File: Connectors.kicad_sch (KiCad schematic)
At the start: 3 parts, among them J1 A, J2 B, J3 C

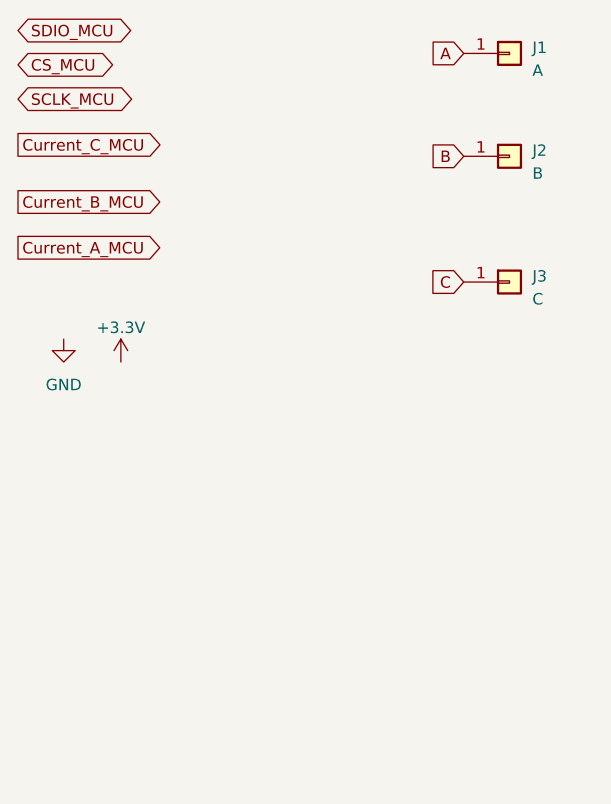
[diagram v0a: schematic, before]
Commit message: Изменил контур под новую крышку
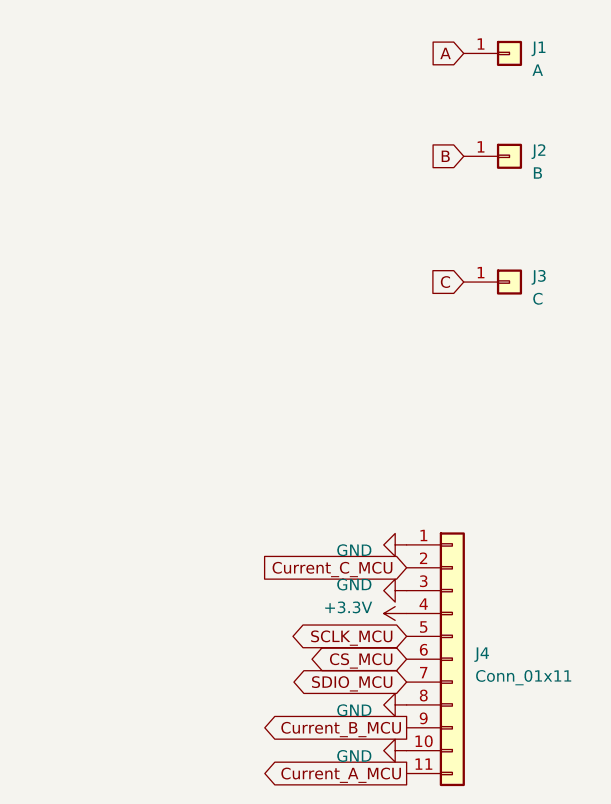
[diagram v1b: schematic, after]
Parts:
- added J4: Conn_01x11, Connector_PinHeader_2.54mm:PinHeader_1x11_P2.54mm_Vertical, symbol Connector_Generic:Conn_01x11
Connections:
- net +3.3V: now also J4.4 (Pin_4)
- net CS_MCU: now also J4.6 (Pin_6)
- net Current_A_MCU: now also J4.11 (Pin_11)
- net Current_B_MCU: now also J4.9 (Pin_9)
- net Current_C_MCU: now also J4.2 (Pin_2)
- net GND: now also J4.1 (Pin_1), J4.10 (Pin_10), J4.3 (Pin_3), J4.8 (Pin_8)
- net SCLK_MCU: now also J4.5 (Pin_5)
- net SDIO_MCU: now also J4.7 (Pin_7)

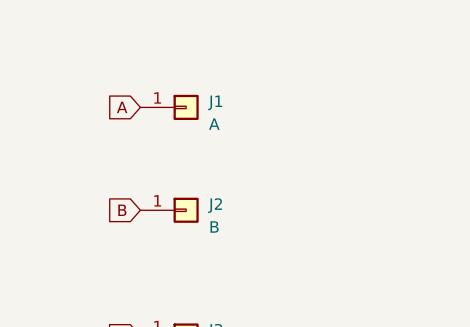
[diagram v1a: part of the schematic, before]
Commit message: Добавил разъёмы под обмотку
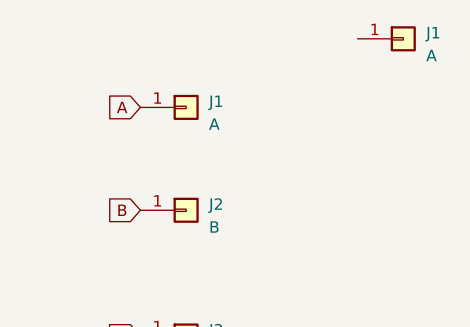
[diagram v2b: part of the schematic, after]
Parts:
- added J1: A, Connector_My:Power_Wire, symbol Connector_Generic:Conn_01x01
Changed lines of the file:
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@@
+    )
+  )
+  (symbol (lib_id "Connector_Generic:Conn_01x01") (at 135.89 73.66 0) (unit 1)
+    (in_bom yes) (on_board yes) (dnp no) (fields_autoplaced)
+    (property "Reference" "J1" (at 138.43 73.025 0)
+      (effects (font (size 1.27 1.27)) (justify left))
+    )
+    (property "Value" "A" (at 138.43 75.565 0)
+      (effects (font (size 1.27 1.27)) (justify left))
+    )
+    (property "Footprint" "Connector_My:Power_Wire" (at 135.89 73.66 0)
+      (effects (font (size 1.27 1.27)) hide)
+    )
+    (property "Datasheet" "~" (at 135.89 73.66 0)
+      (effects (font (size 1.27 1.27)) hide)
+    )
+    (pin "1")
+    (instances
+      (project "Плата датчиков"
+        (path "/69677e3f-3942-4c93-9a5c-92669e2df5eb"
+          (reference "J1") (unit 1)
+        )
+        (path "/69677e3f-3942-4c93-9a5c-92669e2df5eb/000644ca-6534-4b7d-8782-682dfa02d17c"
+          (reference "J5") (unit 1)
+        )
+      )
     )
   )

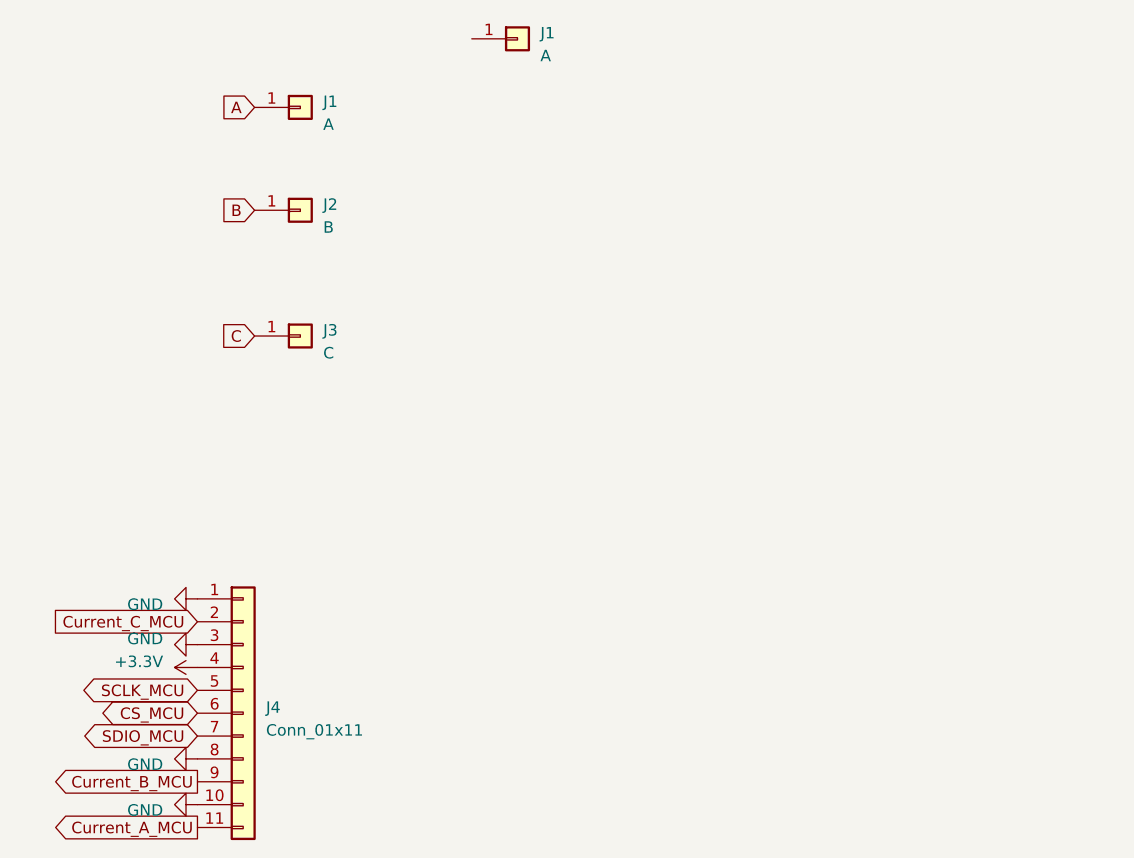
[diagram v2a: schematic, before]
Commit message: Переместил силовые разъёмы
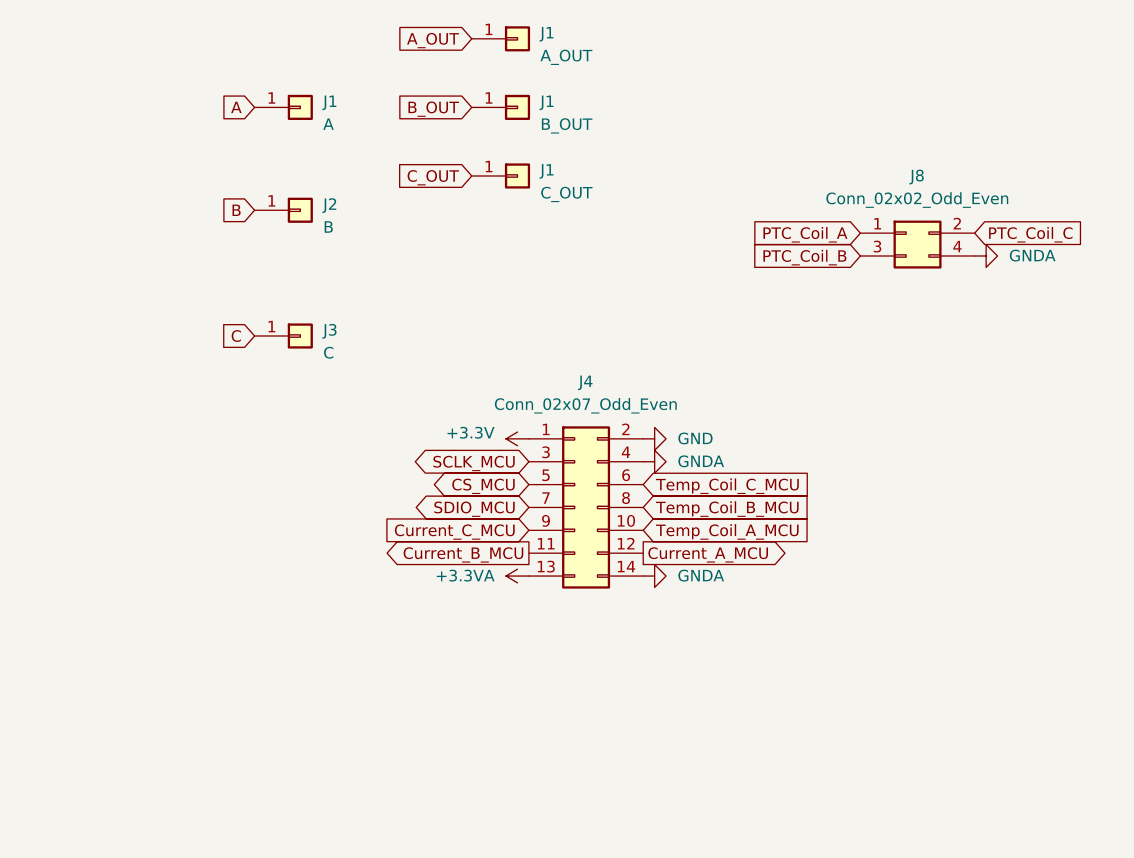
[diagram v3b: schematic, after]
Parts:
- removed J4: Conn_01x11, Connector_PinHeader_2.54mm:PinHeader_1x11_P2.54mm_Vertical, symbol Connector_Generic:Conn_01x11
- added J1: B_OUT, Connector_My:Power_Wire, symbol Connector_Generic:Conn_01x01
- added J1: C_OUT, Connector_My:Power_Wire, symbol Connector_Generic:Conn_01x01
- added J4: Conn_02x07_Odd_Even, Connector_PinSocket_2.54mm:PinSocket_2x07_P2.54mm_Vertical, symbol Connector_Generic:Conn_02x07_Odd_Even
- added J8: Conn_02x02_Odd_Even, Connector_PinHeader_2.54mm:PinHeader_2x02_P2.54mm_Vertical, symbol Connector_Generic:Conn_02x02_Odd_Even
- J1: value A -> A_OUT
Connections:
- net +3.3V: now also J4.1 (Pin_1)
- net CS_MCU: now also J4.5 (Pin_5)
- net Current_A_MCU: now also J4.12 (Pin_12)
- net Current_B_MCU: now also J4.11 (Pin_11)
- net Current_C_MCU: now also J4.9 (Pin_9)
- net GND: now also J4.2 (Pin_2)
- net SCLK_MCU: now also J4.3 (Pin_3)
- net SDIO_MCU: now also J4.7 (Pin_7)
- net A_OUT: now reaches J1.1 (Pin_1)
- new net +3.3VA: J4.13 (Pin_13)
- new net B_OUT: J1.1 (Pin_1)
- new net C_OUT: J1.1 (Pin_1)
- new net GNDA: J4.14 (Pin_14), J4.4 (Pin_4), J8.4 (Pin_4)
- new net PTC_Coil_A: J8.1 (Pin_1)
- new net PTC_Coil_B: J8.3 (Pin_3)
- new net PTC_Coil_C: J8.2 (Pin_2)
- new net Temp_Coil_A_MCU: J4.10 (Pin_10)
- new net Temp_Coil_B_MCU: J4.8 (Pin_8)
- new net Temp_Coil_C_MCU: J4.6 (Pin_6)

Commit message: С ножевыми разъёмами по кругу
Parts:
- removed J1: A_OUT, Connector_My:Power_Wire, symbol Connector_Generic:Conn_01x01
- removed J1: B_OUT, Connector_My:Power_Wire, symbol Connector_Generic:Conn_01x01
- removed J1: C_OUT, Connector_My:Power_Wire, symbol Connector_Generic:Conn_01x01
- added J10, J11, J12, J13, J14, J5, J6, J7, J9: 4900, Connector_My:4900, symbol 4900:4900
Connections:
- net A_OUT: now also J5.1, J5.2, J6.1, J6.2, J9.1, J9.2
- net B_OUT: now also J10.1, J10.2, J11.1, J11.2, J7.1, J7.2
- net C_OUT: now also J12.1, J12.2, J13.1, J13.2, J14.1, J14.2

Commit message: Ещё доработать
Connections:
- net B_OUT: now also J12.1, J12.2, J13.1, J13.2, J14.1, J14.2; no longer J10.1, J10.2, J11.1, J11.2, J7.1, J7.2
- net CS_MCU: now also J4.3 (Pin_3); no longer J4.5 (Pin_5)
- net C_OUT: now also J10.1, J10.2, J11.1, J11.2, J7.1, J7.2; no longer J12.1, J12.2, J13.1, J13.2, J14.1, J14.2
- net Current_C_MCU: now also J4.10 (Pin_10); no longer J4.9 (Pin_9)
- net GNDA: no longer J4.4 (Pin_4)
- net SCLK_MCU: now also J4.5 (Pin_5); no longer J4.3 (Pin_3)
- net Temp_Coil_A_MCU: now also J4.8 (Pin_8); no longer J4.10 (Pin_10)
- net Temp_Coil_B_MCU: now also J4.6 (Pin_6); no longer J4.8 (Pin_8)
- net Temp_Coil_C_MCU: now also J4.4 (Pin_4); no longer J4.6 (Pin_6)
- new net OUT_MCU: J4.9 (Pin_9)

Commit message: Собираю документацию
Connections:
- net GNDA: now also J8.2 (Pin_2); no longer J8.4 (Pin_4)
- net PTC_Coil_B: now also J8.4 (Pin_4); no longer J8.3 (Pin_3)
- net PTC_Coil_C: now also J8.3 (Pin_3); no longer J8.2 (Pin_2)
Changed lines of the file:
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@@
     )
   )
-  (global_label "PTC_Coil_C" (shape input) (at 186.69 95.25 0) (fields_autoplaced)
-    (effects (font (size 1.27 1.27)) (justify left))
-    (property "Intersheetrefs" "${INTERSHEET_REFS}" (at 200.077 95.25 0)
-      (effects (font (size 1.27 1.27)) (justify left) hide)
+  (global_label "PTC_Coil_C" (shape input) (at 173.99 97.79 180) (fields_autoplaced)
+    (effects (font (size 1.27 1.27)) (justify right))
+    (property "Intersheetrefs" "${INTERSHEET_REFS}" (at 160.603 97.79 0)
+      (effects (font (size 1.27 1.27)) (justify right) hide)
     )
   )
@@
     )
   )
-  (global_label "PTC_Coil_B" (shape input) (at 173.99 97.79 180) (fields_autoplaced)
-    (effects (font (size 1.27 1.27)) (justify right))
-    (property "Intersheetrefs" "${INTERSHEET_REFS}" (at 160.603 97.79 0)
-      (effects (font (size 1.27 1.27)) (justify right) hide)
+  (global_label "PTC_Coil_B" (shape input) (at 186.69 97.79 0) (fields_autoplaced)
+    (effects (font (size 1.27 1.27)) (justify left))
+    (property "Intersheetrefs" "${INTERSHEET_REFS}" (at 200.077 97.79 0)
+      (effects (font (size 1.27 1.27)) (justify left) hide)
     )
   )
@@
     )
   )
-  (symbol (lib_id "power:GNDA") (at 186.69 97.79 90) (unit 1)
-    (in_bom yes) (on_board yes) (dnp no) (fields_autoplaced)
-    (property "Reference" "#PWR038" (at 193.04 97.79 0)
-      (effects (font (size 1.27 1.27)) hide)
-    )
-    (property "Value" "GNDA" (at 190.5 97.79 90)
+  (symbol (lib_id "power:GNDA") (at 186.69 95.25 90) (unit 1)
+    (in_bom yes) (on_board yes) (dnp no) (fields_autoplaced)
+    (property "Reference" "#PWR038" (at 193.04 95.25 0)
+      (effects (font (size 1.27 1.27)) hide)
+    )
+    (property "Value" "GNDA" (at 190.5 95.25 90)
       (effects (font (size 1.27 1.27)) (justify right))
     )
-    (property "Footprint" "" (at 186.69 97.79 0)
-      (effects (font (size 1.27 1.27)) hide)
-    )
-    (property "Datasheet" "" (at 186.69 97.79 0)
-      (effects (font (size 1.27 1.27)) hide)
-    )
+    (property "Footprint" "" (at 186.69 95.25 0)
+      (effects (font (size 1.27 1.27)) hide)
+    )
+    (property "Datasheet" "" (at 186.69 95.25 0)
+      (effects (font (size 1.27 1.27)) hide)
+    )

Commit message: ...
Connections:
- net A_OUT: now also J7.1, J7.2; no longer J9.1, J9.2
- net C_OUT: now also J9.1, J9.2; no longer J7.1, J7.2
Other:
- note added: "Межплатные сигнальные разъёмы"
- note added: "Ножевые разъёмы"
- note added: "Фазные разъёмы"
